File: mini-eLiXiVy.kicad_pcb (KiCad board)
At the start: 2 copper layers, 302.2 x 93.5 mm, 175 parts, among them J1 TYPE-C-31-M12_13_EDITED, J2 AVR-ISP-6, SW1 SW_Push, U1 ATmega32U4-AU, U2 WE-TVS-82400102, Y1 Crystal_GND24_Small

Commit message: Reconnected a bunch of unconncted lines
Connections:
- net REA+ renamed REA
- net REA- renamed REB
- MX_'1 pad 1: COL11 -> Net-(MX_'1-Pad1)
- MX_,1 pad 1: COL9 -> Net-(MX_,1-Pad1)
- MX_.1 pad 1: COL10 -> Net-(MX_.1-Pad1)
- MX_/1 pad 1: COL11 -> Net-(MX_/1-Pad1)
- MX_1 pad 1: COL1 -> Net-(MX_1-Pad1)
- MX_1.25U_FN1 pad 2: Net-(D64-Pad2) -> Net-(MX_1.25U_FN1-Pad2)
- MX_1.25U_R_CTRL1 pad 2: Net-(D63-Pad2) -> Net-(MX_1.25U_R_CTRL1-Pad2)
- MX_1.5U_TAB1 pad 1: COL0 -> Net-(MX_1.5U_TAB1-Pad1)
- MX_1.5U_\1 pad 2: Net-(D28-Pad2) -> Net-(MX_1.5U_\1-Pad2)
- MX_1.75U_CAPSLOCK1 pad 2: Net-(D30-Pad2) -> Net-(MX_1.75U_CAPSLOCK1-Pad2)
- MX_1.75U__RSHIFT1 pad 1: COL12 -> Net-(MX_1.75U__RSHIFT1-Pad1)
- MX_2 pad 1: COL2 -> Net-(MX_2-Pad1)
- MX_2.25U_ENTER1 pad 2: Net-(D42-Pad2) -> Net-(MX_2.25U_ENTER1-Pad2)
- MX_2.25U_LSHIFT1 pad 2: Net-(D44-Pad2) -> Net-(MX_2.25U_LSHIFT1-Pad2)
- MX_2U_BACKSP1 pad 1: COL13 -> Net-(MX_2U_BACKSP1-Pad1)
- MX_3 pad 1: COL3 -> Net-(MX_3-Pad1)
- MX_4 pad 1: COL4 -> Net-(MX_4-Pad1)
- MX_5 pad 1: COL5 -> Net-(MX_5-Pad1)
- MX_6 pad 1: COL6 -> Net-(MX_6-Pad1)
- MX_7 pad 1: COL7 -> Net-(MX_7-Pad1)
- MX_8 pad 1: COL8 -> Net-(MX_8-Pad1)
- MX_;1 pad 1: COL10 -> Net-(MX_;1-Pad1)
- MX_A1 pad 1: COL1 -> Net-(MX_A1-Pad1)
- MX_ARR_U1 pad 1: COL13 -> Net-(MX_ARR_U1-Pad1)
- MX_B1 pad 1: COL6 -> Net-(MX_B1-Pad1)
- MX_D1 pad 1: COL3 -> Net-(MX_D1-Pad1)
- MX_DASH1 pad 1: COL11 -> Net-(MX_DASH1-Pad1)
- MX_DEL1 pad 1: COL14 -> Net-(MX_DEL1-Pad1)
- MX_E1 pad 1: COL3 -> Net-(MX_E1-Pad1)
- MX_EQUALS1 pad 1: COL12 -> Net-(MX_EQUALS1-Pad1)
- MX_ESC1 pad 1: COL0 -> Net-(MX_ESC1-Pad1)
- MX_F1 pad 1: COL4 -> Net-(MX_F1-Pad1)
- MX_G1 pad 1: COL5 -> Net-(MX_G1-Pad1)
- MX_H1 pad 1: COL6 -> Net-(MX_H1-Pad1)
- MX_I1 pad 1: COL8 -> Net-(MX_I1-Pad1)
- MX_INS1 pad 1: COL14 -> Net-(MX_INS1-Pad1)
- MX_J1 pad 1: COL7 -> Net-(MX_J1-Pad1)
- MX_K1 pad 1: COL8 -> Net-(MX_K1-Pad1)
- MX_L1 pad 1: COL9 -> Net-(MX_L1-Pad1)
- MX_L_BSLASH1 pad 1: COL1 -> Net-(MX_L_BSLASH1-Pad1)
- MX_O1 pad 1: COL9 -> Net-(MX_O1-Pad1)
- MX_P1 pad 1: COL10 -> Net-(MX_P1-Pad1)
- MX_Q1 pad 1: COL1 -> Net-(MX_Q1-Pad1)
- MX_R1 pad 1: COL4 -> Net-(MX_R1-Pad1)
- MX_S1 pad 1: COL2 -> Net-(MX_S1-Pad1)
- MX_T1 pad 1: COL5 -> Net-(MX_T1-Pad1)
- MX_TEMP1 pad 1: COL14 -> Net-(MX_TEMP1-Pad1)
- MX_U1 pad 1: COL7 -> Net-(MX_U1-Pad1)
- MX_W1 pad 1: COL2 -> Net-(MX_W1-Pad1)
- MX_Y1 pad 1: COL6 -> Net-(MX_Y1-Pad1)
- MX_Z1 pad 1: COL2 -> Net-(MX_Z1-Pad1)
- MX_[1 pad 1: COL11 -> Net-(MX_[1-Pad1)
- MX_]1 pad 1: COL12 -> Net-(MX_]1-Pad1)
- R5 pad 2: Net-(J1-Pad4) -> Net-(R5-Pad2)
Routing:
- net Net-(D45-Pad2): track 0.00 -> 9.69 mm

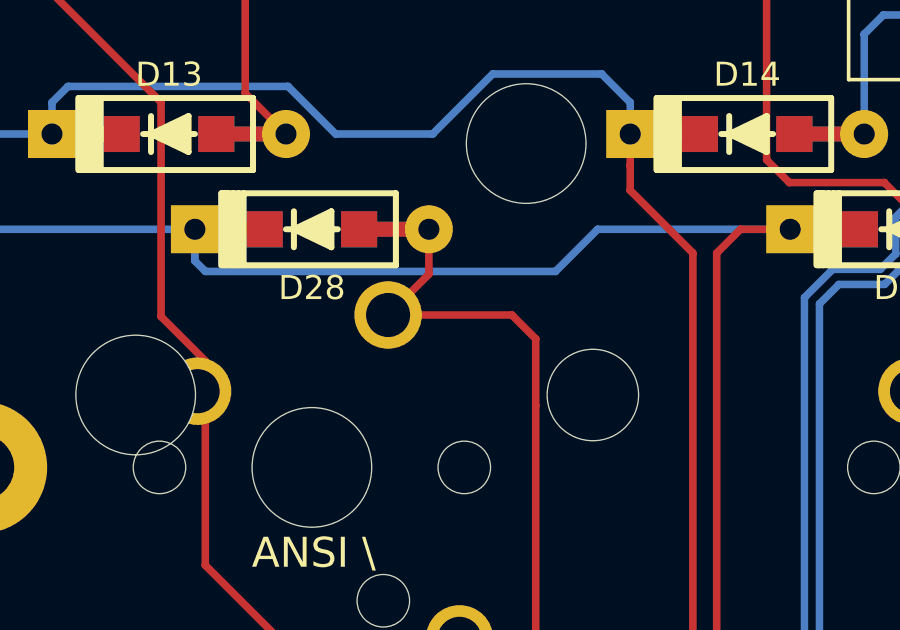
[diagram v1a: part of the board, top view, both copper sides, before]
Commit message: Reconnected some unconnected switches
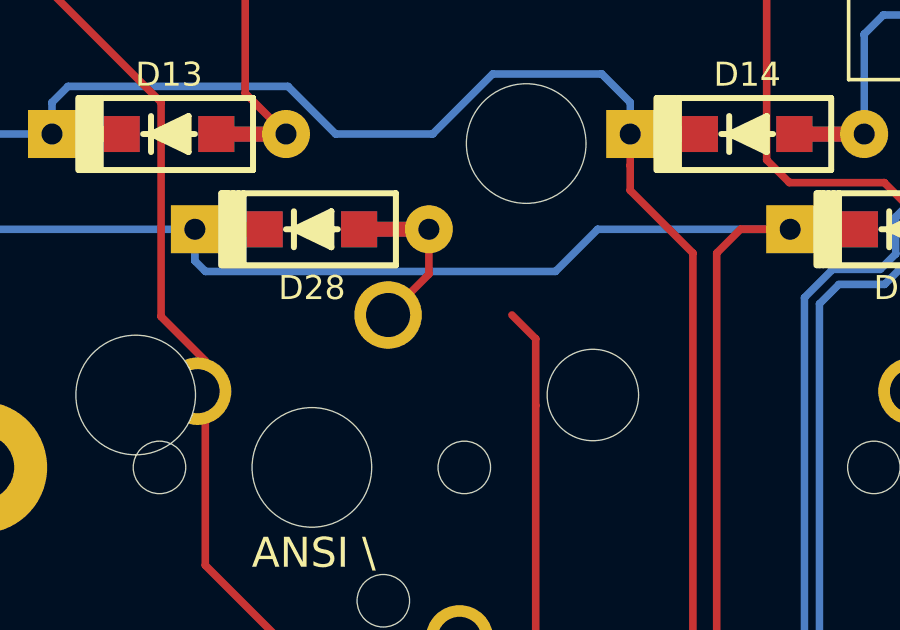
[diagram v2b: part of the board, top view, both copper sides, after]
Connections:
- net DN renamed Net-(R3-Pad1)
- net DP renamed Net-(R2-Pad1)
- MX_'1 pad 1: Net-(MX_'1-Pad1) -> COL11
- MX_,1 pad 1: Net-(MX_,1-Pad1) -> COL9
- MX_.1 pad 1: Net-(MX_.1-Pad1) -> COL10
- MX_/1 pad 1: Net-(MX_/1-Pad1) -> COL11
- MX_1 pad 1: Net-(MX_1-Pad1) -> COL1
- MX_1.25U_FN1 pad 2: Net-(MX_1.25U_FN1-Pad2) -> Net-(D64-Pad2)
- MX_1.25U_R_CTRL1 pad 2: Net-(MX_1.25U_R_CTRL1-Pad2) -> Net-(D63-Pad2)
- MX_1.5U_TAB1 pad 1: Net-(MX_1.5U_TAB1-Pad1) -> COL0
- MX_1.75U_CAPSLOCK1 pad 2: Net-(MX_1.75U_CAPSLOCK1-Pad2) -> Net-(D30-Pad2)
- MX_1.75U__RSHIFT1 pad 1: Net-(MX_1.75U__RSHIFT1-Pad1) -> COL12
- MX_2 pad 1: Net-(MX_2-Pad1) -> COL2
- MX_2.25U_ENTER1 pad 2: Net-(MX_2.25U_ENTER1-Pad2) -> Net-(D42-Pad2)
- MX_2.25U_LSHIFT1 pad 2: Net-(MX_2.25U_LSHIFT1-Pad2) -> Net-(D44-Pad2)
- MX_2U_BACKSP1 pad 1: Net-(MX_2U_BACKSP1-Pad1) -> COL13
- MX_3 pad 1: Net-(MX_3-Pad1) -> COL3
- MX_4 pad 1: Net-(MX_4-Pad1) -> COL4
- MX_5 pad 1: Net-(MX_5-Pad1) -> COL5
- MX_6 pad 1: Net-(MX_6-Pad1) -> COL6
- MX_7 pad 1: Net-(MX_7-Pad1) -> COL7
- MX_8 pad 1: Net-(MX_8-Pad1) -> COL8
- MX_;1 pad 1: Net-(MX_;1-Pad1) -> COL10
- MX_A1 pad 1: Net-(MX_A1-Pad1) -> COL1
- MX_ARR_U1 pad 1: Net-(MX_ARR_U1-Pad1) -> COL13
- MX_B1 pad 1: Net-(MX_B1-Pad1) -> COL6
- MX_D1 pad 1: Net-(MX_D1-Pad1) -> COL3
- MX_DASH1 pad 1: Net-(MX_DASH1-Pad1) -> COL11
- MX_DEL1 pad 1: Net-(MX_DEL1-Pad1) -> COL14
- MX_E1 pad 1: Net-(MX_E1-Pad1) -> COL3
- MX_EQUALS1 pad 1: Net-(MX_EQUALS1-Pad1) -> COL12
- MX_ESC1 pad 1: Net-(MX_ESC1-Pad1) -> COL0
- MX_F1 pad 1: Net-(MX_F1-Pad1) -> COL4
- MX_G1 pad 1: Net-(MX_G1-Pad1) -> COL5
- MX_H1 pad 1: Net-(MX_H1-Pad1) -> COL6
- MX_I1 pad 1: Net-(MX_I1-Pad1) -> COL8
- MX_INS1 pad 1: Net-(MX_INS1-Pad1) -> COL14
- MX_J1 pad 1: Net-(MX_J1-Pad1) -> COL7
- MX_K1 pad 1: Net-(MX_K1-Pad1) -> COL8
- MX_L1 pad 1: Net-(MX_L1-Pad1) -> COL9
- MX_L_BSLASH1 pad 1: Net-(MX_L_BSLASH1-Pad1) -> COL1
- MX_O1 pad 1: Net-(MX_O1-Pad1) -> COL9
- MX_P1 pad 1: Net-(MX_P1-Pad1) -> COL10
- MX_Q1 pad 1: Net-(MX_Q1-Pad1) -> COL1
- MX_R1 pad 1: Net-(MX_R1-Pad1) -> COL4
- MX_S1 pad 1: Net-(MX_S1-Pad1) -> COL2
- MX_T1 pad 1: Net-(MX_T1-Pad1) -> COL5
- MX_TEMP1 pad 1: Net-(MX_TEMP1-Pad1) -> COL14
- MX_U1 pad 1: Net-(MX_U1-Pad1) -> COL7
- MX_W1 pad 1: Net-(MX_W1-Pad1) -> COL2
- MX_Y1 pad 1: Net-(MX_Y1-Pad1) -> COL6
- MX_Z1 pad 1: Net-(MX_Z1-Pad1) -> COL2
- MX_[1 pad 1: Net-(MX_[1-Pad1) -> COL11
- MX_]1 pad 1: Net-(MX_]1-Pad1) -> COL12
- R5 pad 2: Net-(R5-Pad2) -> Net-(J1-Pad4)
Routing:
- net Net-(D28-Pad2): track 25.0 -> 20.9 mm

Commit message: Edited README and made the final gerber files
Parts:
- moved D37 63.9 mm to (169.9, 54.8)
- moved D42 63.9 mm to (277.0, 54.8)
- moved D43 63.9 mm to (304.0, 54.8)
- moved D54 63.9 mm to (217.5, 73.8)
- moved D57 63.9 mm to (288.9, 73.8)
- moved D58 63.9 mm to (304.0, 73.8)
- moved MX_2.25U_ENTER1 63.9 mm to (277.0, 62.7)
- moved MX_INS1 63.9 mm to (308.0, 62.7)
- moved MX_ISO_\1 63.9 mm to (265.1, 62.7)
- moved MX_J1 63.9 mm to (169.9, 62.7)
- moved C1 63.9 mm to (121.2, 96.6)
- moved C8 63.9 mm to (26.2, 28.3)
- moved D14 63.9 mm to (298.7, 32.5)
- moved D26 63.9 mm to (241.3, 35.7)
- moved D27 63.9 mm to (260.4, 35.7)
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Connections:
- MX_1.5U_\1 pad 2: Net-(MX_1.5U_\1-Pad2) -> Net-(D28-Pad2)
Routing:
- net Net-(D28-Pad2): track 20.9 -> 25.0 mm

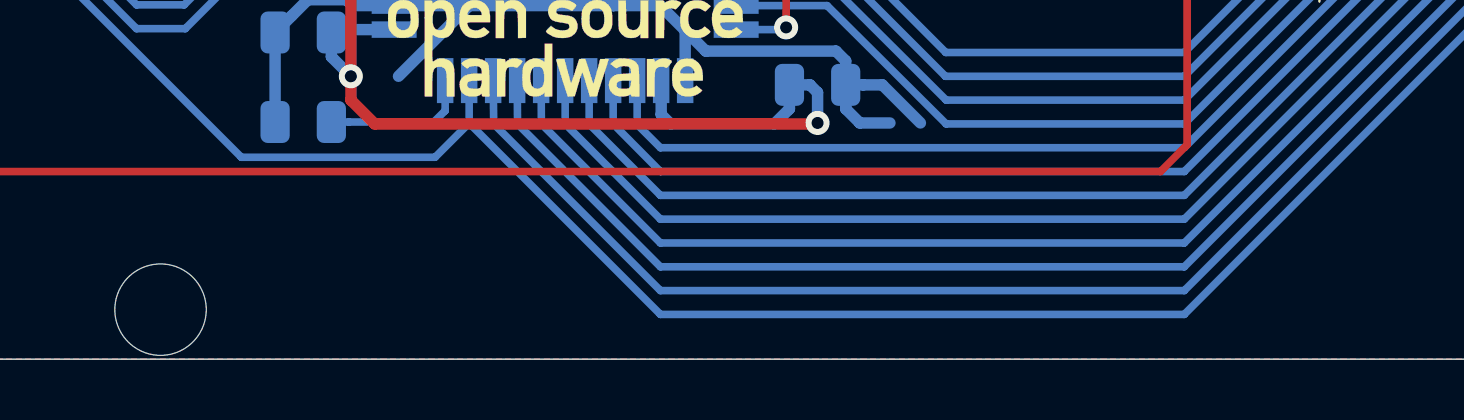
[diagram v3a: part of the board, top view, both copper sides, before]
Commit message: Added OHL license silkscreen.
Added a "Licensed under CERN-OHL-S v2" silkscreen to the PCB, as per CERN-OHL-S v2, section 2.2.9.
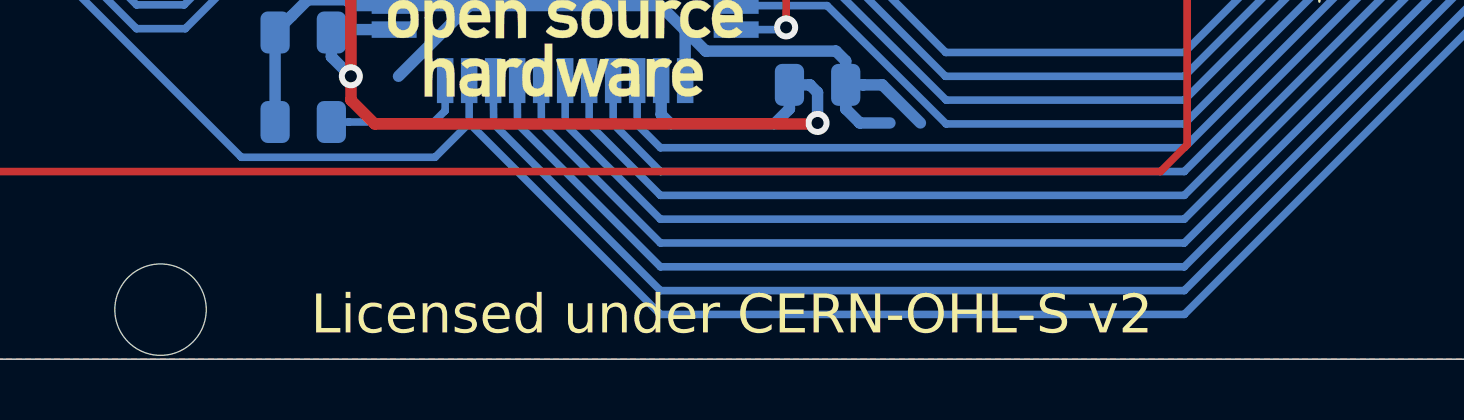
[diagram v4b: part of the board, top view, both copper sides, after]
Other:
- board text added: "Licensed under CERN-OHL-S v2"
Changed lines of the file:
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@@
   (general
     (thickness 1.6)
-    (drawings 24)
+    (drawings 25)
     (tracks 1406)
     (zones 0)
@@
     )
   )
+  (gr_text "Licensed under CERN-OHL-S v2" (at 112.7125 107.95) (layer F.SilkS)
+    (effects (font (size 1.3 1.3) (thickness 0.2)))
+  )
   (gr_text RESET (at 40.5384 66.07429) (layer B.SilkS)
     (effects (font (size 1 1) (thickness 0.15)) (justify mirror))
@@
   (segment (start 310.515 17.69195) (end 310.45405 17.631) (width 0.254) (layer B.Cu) (net 114))
   (segment (start 310.515 19.52625) (end 310.515 17.69195) (width 0.254) (layer B.Cu) (net 114))
-  (via (at 31.767 34.46675) (size 0.8) (drill 0.4) (layers F.Cu B.Cu) (net 117))
-  (segment (start 32.512 32.63035) (end 31.492 33.65035) (width 0.25) (layer B.Cu) (net 117))
-  (segment (start 31.492 33.65035) (end 31.492 34.19175) (width 0.25) (layer B.Cu) (net 117))
-  (segment (start 31.492 34.19175) (end 31.767 34.46675) (width 0.25) (layer B.Cu) (net 117))
-  (via (at 42.78425 74.549) (size 0.8) (drill 0.4) (layers F.Cu B.Cu) (net 117))
-  (segment (start 45.410804 78.236) (end 51.602054 78.236) (width 0.25) (layer B.Cu) (net 117))
-  (segment (start 42.50925 75.334446) (end 45.410804 78.236) (width 0.25) (layer B.Cu) (net 117))
-  (segment (start 57.571054 84.205) (end 103.608554 84.205) (width 0.25) (layer B.Cu) (net 117))
-  (segment (start 42.78425 74.549) (end 42.50925 74.824) (width 0.25) (layer B.Cu) (net 117))
-  (segment (start 51.602054 78.236) (end 57.571054 84.205) (width 0.25) (layer B.Cu) (net 117))
-  (segment (start 105.40625 86.002696) (end 105.40625 87.481249) (width 0.25) (layer B.Cu) (net 117))
-  (segment (start 105.55625 87.631249) (end 105.55625 88.75625) (width 0.25) (layer B.Cu) (net 117))
-  (segment (start 103.608554 84.205) (end 105.40625 86.002696) (width 0.25) (layer B.Cu) (net 117))
-  (segment (start 42.50925 74.824) (end 42.50925 75.334446) (width 0.25) (layer B.Cu) (net 117))
-  (segment (start 105.40625 87.481249) (end 105.55625 87.631249) (width 0.25) (layer B.Cu) (net 117))
-  (segment (start 31.492 34.74175) (end 31.767 34.46675) (width 0.25) (layer F.Cu) (net 117))
-  (segment (start 31.492 35.107196) (end 31.492 34.74175) (width 0.25) (layer F.Cu) (net 117))
-  (segment (start 35.822304 39.4375) (end 31.492 35.107196) (width 0.25) (layer F.Cu) (net 117))
-  (segment (start 42.78425 74.549) (end 42.50925 74.274) (width 0.25) (layer F.Cu) (net 117))
-  (segment (start 42.50925 74.274) (end 42.50925 40.568196) (width 0.25) (layer F.Cu) (net 117))
-  (segment (start 42.50925 40.568196) (end 41.378554 39.4375) (width 0.25) (layer F.Cu) (net 117))
-  (segment (start 41.378554 39.4375) (end 35.822304 39.4375) (width 0.25) (layer F.Cu) (net 117))
-  (segment (start 30.992 33.65035) (end 30.992 34.19175) (width 0.25) (layer B.Cu) (net 118))
-  (segment (start 30.992 34.19175) (end 30.717 34.46675) (width 0.25) (layer B.Cu) (net 118))
-  (via (at 30.717 34.46675) (size 0.8) (drill 0.4) (layers F.Cu B.Cu) (net 118))
-  (segment (start 29.972 32.63035) (end 30.992 33.65035) (width 0.25) (layer B.Cu) (net 118))
-  (via (at 41.73425 74.549) (size 0.8) (drill 0.4) (layers F.Cu B.Cu) (net 118))
-  (segment (start 104.75625 87.631249) (end 104.75625 88.75625) (width 0.25) (layer B.Cu) (net 118))
-  (segment (start 104.90625 86.209804) (end 104.90625 87.481249) (width 0.25) (layer B.Cu) (net 118))
-  (segment (start 51.394946 78.736) (end 57.363946 84.705) (width 0.25) (layer B.Cu) (net 118))
-  (segment (start 104.90625 87.481249) (end 104.75625 87.631249) (width 0.25) (layer B.Cu) (net 118))
-  (segment (start 57.363946 84.705) (end 103.401446 84.705) (width 0.25) (layer B.Cu) (net 118))
-  (segment (start 103.401446 84.705) (end 104.90625 86.209804) (width 0.25) (layer B.Cu) (net 118))
-  (segment (start 42.00925 74.824) (end 42.00925 75.541554) (width 0.25) (layer B.Cu) (net 118))
-  (segment (start 42.00925 75.541554) (end 45.203696 78.736) (width 0.25) (layer B.Cu) (net 118))
-  (segment (start 41.73425 74.549) (end 42.00925 74.824) (width 0.25) (layer B.Cu) (net 118))
-  (segment (start 45.203696 78.736) (end 51.394946 78.736) (width 0.25) (layer B.Cu) (net 118))
-  (segment (start 35.615196 39.9375) (end 30.992 35.314304) (width 0.25) (layer F.Cu) (net 118))
-  (segment (start 42.00925 74.274) (end 42.00925 40.775304) (width 0.25) (layer F.Cu) (net 118))
-  (segment (start 41.73425 74.549) (end 42.00925 74.274) (width 0.25) (layer F.Cu) (net 118))
-  (segment (start 30.992 35.314304) (end 30.992 34.74175) (width 0.25) (layer F.Cu) (net 118))
-  (segment (start 41.171446 39.9375) (end 35.615196 39.9375) (width 0.25) (layer F.Cu) (net 118))
-  (segment (start 30.992 34.74175) (end 30.717 34.46675) (width 0.25) (layer F.Cu) (net 118))
-  (segment (start 42.00925 40.775304) (end 41.171446 39.9375) (width 0.25) (layer F.Cu) (net 118))
   (segment (start 115.8875 68.2625) (end 115.8875 83.34375) (width 0.254) (layer F.Cu) (net 115))
   (segment (start 112.7125 83.36875) (end 115.8625 83.36875) (width 0.254) (layer B.Cu) (net 115))
@@
   (segment (start 127.79375 68.2625) (end 128.0875 67.96875) (width 0.25) (layer B.Cu) (net 116))
   (segment (start 294.235554 56.60625) (end 303.316054 56.60625) (width 0.25) (layer B.Cu) (net 116))
+  (via (at 31.767 34.46675) (size 0.8) (drill 0.4) (layers F.Cu B.Cu) (net 117))
+  (segment (start 32.512 32.63035) (end 31.492 33.65035) (width 0.25) (layer B.Cu) (net 117))
+  (segment (start 31.492 33.65035) (end 31.492 34.19175) (width 0.25) (layer B.Cu) (net 117))
+  (segment (start 31.492 34.19175) (end 31.767 34.46675) (width 0.25) (layer B.Cu) (net 117))
+  (via (at 42.78425 74.549) (size 0.8) (drill 0.4) (layers F.Cu B.Cu) (net 117))
+  (segment (start 45.410804 78.236) (end 51.602054 78.236) (width 0.25) (layer B.Cu) (net 117))
+  (segment (start 42.50925 75.334446) (end 45.410804 78.236) (width 0.25) (layer B.Cu) (net 117))
+  (segment (start 57.571054 84.205) (end 103.608554 84.205) (width 0.25) (layer B.Cu) (net 117))
+  (segment (start 42.78425 74.549) (end 42.50925 74.824) (width 0.25) (layer B.Cu) (net 117))
+  (segment (start 51.602054 78.236) (end 57.571054 84.205) (width 0.25) (layer B.Cu) (net 117))
+  (segment (start 105.40625 86.002696) (end 105.40625 87.481249) (width 0.25) (layer B.Cu) (net 117))
+  (segment (start 105.55625 87.631249) (end 105.55625 88.75625) (width 0.25) (layer B.Cu) (net 117))
+  (segment (start 103.608554 84.205) (end 105.40625 86.002696) (width 0.25) (layer B.Cu) (net 117))
+  (segment (start 42.50925 74.824) (end 42.50925 75.334446) (width 0.25) (layer B.Cu) (net 117))
+  (segment (start 105.40625 87.481249) (end 105.55625 87.631249) (width 0.25) (layer B.Cu) (net 117))
+  (segment (start 31.492 34.74175) (end 31.767 34.46675) (width 0.25) (layer F.Cu) (net 117))
+  (segment (start 31.492 35.107196) (end 31.492 34.74175) (width 0.25) (layer F.Cu) (net 117))
+  (segment (start 35.822304 39.4375) (end 31.492 35.107196) (width 0.25) (layer F.Cu) (net 117))
+  (segment (start 42.78425 74.549) (end 42.50925 74.274) (width 0.25) (layer F.Cu) (net 117))
+  (segment (start 42.50925 74.274) (end 42.50925 40.568196) (width 0.25) (layer F.Cu) (net 117))
+  (segment (start 42.50925 40.568196) (end 41.378554 39.4375) (width 0.25) (layer F.Cu) (net 117))
+  (segment (start 41.378554 39.4375) (end 35.822304 39.4375) (width 0.25) (layer F.Cu) (net 117))
+  (segment (start 30.992 33.65035) (end 30.992 34.19175) (width 0.25) (layer B.Cu) (net 118))
+  (segment (start 30.992 34.19175) (end 30.717 34.46675) (width 0.25) (layer B.Cu) (net 118))
+  (via (at 30.717 34.46675) (size 0.8) (drill 0.4) (layers F.Cu B.Cu) (net 118))
+  (segment (start 29.972 32.63035) (end 30.992 33.65035) (width 0.25) (layer B.Cu) (net 118))
+  (via (at 41.73425 74.549) (size 0.8) (drill 0.4) (layers F.Cu B.Cu) (net 118))
+  (segment (start 104.75625 87.631249) (end 104.75625 88.75625) (width 0.25) (layer B.Cu) (net 118))
+  (segment (start 104.90625 86.209804) (end 104.90625 87.481249) (width 0.25) (layer B.Cu) (net 118))
+  (segment (start 51.394946 78.736) (end 57.363946 84.705) (width 0.25) (layer B.Cu) (net 118))
+  (segment (start 104.90625 87.481249) (end 104.75625 87.631249) (width 0.25) (layer B.Cu) (net 118))
+  (segment (start 57.363946 84.705) (end 103.401446 84.705) (width 0.25) (layer B.Cu) (net 118))
+  (segment (start 103.401446 84.705) (end 104.90625 86.209804) (width 0.25) (layer B.Cu) (net 118))
+  (segment (start 42.00925 74.824) (end 42.00925 75.541554) (width 0.25) (layer B.Cu) (net 118))
+  (segment (start 42.00925 75.541554) (end 45.203696 78.736) (width 0.25) (layer B.Cu) (net 118))
+  (segment (start 41.73425 74.549) (end 42.00925 74.824) (width 0.25) (layer B.Cu) (net 118))
+  (segment (start 45.203696 78.736) (end 51.394946 78.736) (width 0.25) (layer B.Cu) (net 118))
+  (segment (start 35.615196 39.9375) (end 30.992 35.314304) (width 0.25) (layer F.Cu) (net 118))
+  (segment (start 42.00925 74.274) (end 42.00925 40.775304) (width 0.25) (layer F.Cu) (net 118))
+  (segment (start 41.73425 74.549) (end 42.00925 74.274) (width 0.25) (layer F.Cu) (net 118))
+  (segment (start 30.992 35.314304) (end 30.992 34.74175) (width 0.25) (layer F.Cu) (net 118))
+  (segment (start 41.171446 39.9375) (end 35.615196 39.9375) (width 0.25) (layer F.Cu) (net 118))
+  (segment (start 30.992 34.74175) (end 30.717 34.46675) (width 0.25) (layer F.Cu) (net 118))
+  (segment (start 42.00925 40.775304) (end 41.171446 39.9375) (width 0.25) (layer F.Cu) (net 118))
   (zone (net 1) (net_name GND) (layer F.Cu) (hatch edge 0.508)
     (connect_pads (clearance 0.508))

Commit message: Tweaked silkscreen
Changed silkscreen layer for certain keyswitches, so it can be seen from the back what locations need to be used
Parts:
- C8: value 100nF -> 0.1uF
- J2: moved to F.Cu
- LO0: footprint mini-Logos:eLiXiVy-SilkScreenv2 -> mini-Logos:eLiXiVy-SilkScreen-rev1
- MX_PrtSc1: footprint mini-MX-Tweaks:MXOnly-1U-NoLED-3Pin_tweak -> mini-MX-Tweaks:MXOnly-1U-NoLED_tweak
- moved D62 11.8 mm to (152.4, 100.8), turned to 270 degrees
- moved D13 6.41 mm to (273.8, 35.7)
- moved J2 2.44 mm to (125.5, 90.8), turned to 0 degrees
- moved D1 1.59 mm to (42.9, 32.5)
- moved C1 1.02 mm to (120.2, 96.6)
- moved C2 1.02 mm to (120.2, 90.2)
- moved Y1 1.02 mm to (120.2, 93.4)
- moved D12 0.79 mm to (250.0, 32.5)
- moved C4 0.38 mm to (116.0, 92.0)
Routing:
- net +5V: track 234.7 -> 250.6 mm
- net Net-(D12-Pad2): track 13.6 -> 0.00 mm
- net Net-(D62-Pad2): track 3.42 -> 14.8 mm
- net GND: track 152.1 -> 161.7 mm
- net COL14: track 310.1 -> 302.0 mm
- net RESET: track 161.3 -> 154.2 mm
- net ROW4: track 316.5 -> 321.4 mm
- net COL13: track 283.1 -> 287.9 mm
- net Net-(D13-Pad2): track 13.6 -> 17.9 mm
- net SCK: track 30.4 -> 33.8 mm
- net MOSI: track 29.8 -> 27.5 mm
- net MISO: track 21.9 -> 19.6 mm
- net XTAL2: track 16.4 -> 14.7 mm
- net XTAL1: track 9.68 -> 8.67 mm
- net ROW0: track 566.8 -> 566.0 mm
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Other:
- board text removed: "JLCJLCJLCJLC"
